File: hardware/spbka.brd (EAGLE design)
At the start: 33 x 20.3 mm, 20 parts, among them Q1 DMP1045U-7, U1 ATTINY10, U2 LM4041DYM3-1.2, U3 MCP6L01T

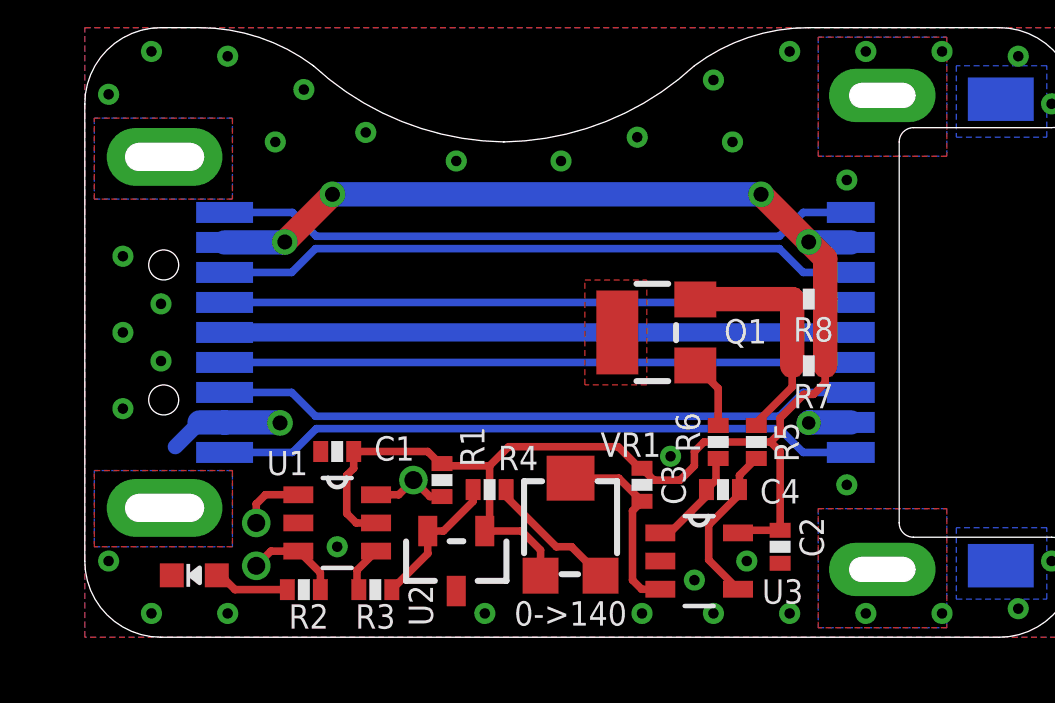
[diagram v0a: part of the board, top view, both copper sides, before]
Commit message: Some small changes, HW v1.2
Hardware bumped to v1.2:
Added unmasked vias for VCC and GND to make it easier to program.
Made USB3 socket pads longer (some components and things had to be moved slightly for this).
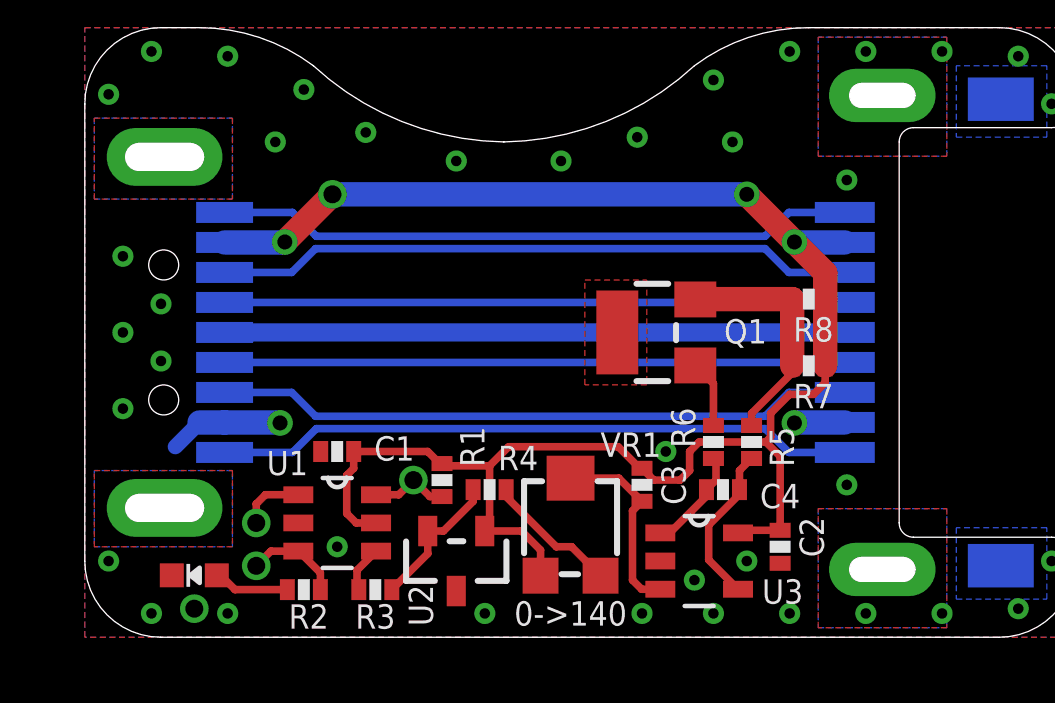
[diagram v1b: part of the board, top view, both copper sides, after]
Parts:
- moved R5 0.16 mm to (28.6, 33.2)
- moved R6 0.16 mm to (27.3, 33.2)
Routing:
- net GND: track 5.25 -> 5.52 mm, vias 40 -> 41
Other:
- board text added: "200411 1.2"
- board text removed: "190909 1.1"

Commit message: hardware v2.1
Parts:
- removed CN1: (no value), zak:USB-3-TYPE-A-SMD-PLUG-SLOT
- removed CN2: (no value), zak:USB-3-TYPE-A-SMD-SOCKET-SLOT
- removed U3: MCP6L01T, zak:SOT23-5_SM_PAD
- added Q2: MMBT4401 / MMBT3904, microbuilder:SOT23-R
- added R10: 10k, zak:0402_XSMALL
- added R11: 1k, zak:0402_XSMALL
- added R12: 1M, zak:0402_XSMALL
- added R9: 47k, zak:0402_XSMALL
- added USB1: USB-TYPE-AHORZ, zak:USB-TYPE-A
- added USB2: (no value), zak:USB-TYPE-A-PLUG-SLOT
- added VR2: 5k, zak:TRIMPOT_BOURNS3MM
- C1, C2, C3, C4, R2, R5, R6, R7, R8: device zak:0402_SMALL -> zak:0402_XSMALL
- Q1: value DMP1045U-7 -> DMP1045U-7 / DMP2035U-7
- R1: value 3k9 -> 10k; device zak:0402_SMALL -> zak:0402_XSMALL
- R3: value 3k9 -> 1k; device zak:0402_SMALL -> zak:0402_XSMALL
- R4: value 3k9 -> 0R; device zak:0402_SMALL -> zak:0402_XSMALL
- U2: value LM4041DYM3-1.2 -> MCP6L01T / MCP6001T; device zak:SOT-23-SLIMPAD -> zak:SOT23-5_SM_PAD
- moved U2 14.9 mm to (25.8, 42.3)
- moved R3 12.3 mm to (26.7, 34.3)
- moved R7 11.1 mm to (20.4, 40.4), turned to 0 degrees
- moved U1 11.1 mm to (13.4, 41.5), turned to 270 degrees
- moved C2 11.0 mm to (25.8, 40.0), turned to 180 degrees
- moved R2 10.3 mm to (8.30, 37.0), turned to 90 degrees
- moved R8 10.1 mm to (20.4, 38.8), turned to 0 degrees
- moved C1 8.90 mm to (15.8, 41.7), turned to 270 degrees
- moved LED1 8.79 mm to (7.00, 37.0), turned to 180 degrees
- moved VR1 8.45 mm to (14.1, 30.6), turned to 90 degrees
- moved R1 8.17 mm to (15.8, 39.7)
- moved R6 7.09 mm to (22.4, 38.3), turned to 270 degrees
- moved R4 7.02 mm to (26.7, 33.1), turned to 180 degrees
- moved R5 6.75 mm to (24.7, 38.7), turned to 180 degrees
- moved C4 6.59 mm to (24.7, 37.5)
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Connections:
- removed net N$13: R3.1, U1.4
- removed net N$14: CN1.SSTX-, CN2.SSTX-
- removed net N$15: CN1.D+, CN2.D+
- removed net N$16: CN1.D-, CN2.D-
- removed net N$19: C1.2, C2.2, C3.2, CN1.VBUS, CN2.VBUS, R1.2, R7.1, R8.1, U1.5, U2.1, U3.5, VR1.1
- removed net N$9 (its old number): CN1.SSRX-, CN2.SSRX-
- new net N$1: Q2.2, R3.2, R4.1
- new net VBUS: C1.2, C2.2, C3.2, Q2.1, Q2.3, R1.2, R10.2, R11.2, R7.1, R8.1, R9.2, U1.5, U2.5, USB1.VCC, USB2.VBUS, VR1.1
- net GND: now also U2.2, USB1.GND, USB1.SHIELD1, USB1.SHIELD2, USB2.GND, USB2.PAD1, USB2.PAD2; no longer CN1.GND, CN1.PAD1, CN1.PAD2, CN2.GND, CN2.PAD1, CN2.PAD2, CN2.PAD3, CN2.PAD4, U3.2
- net N$11: now also R12.2, R9.1, U2.3; no longer U3.3
- net N$12: now also R11.1, VR2.1; no longer CN1.SSTX+, CN2.SSTX+
- net N$3: now also U2.1; no longer U3.1
- net N$5: now also USB1.D+, USB2.D+; no longer CN1.GND_DRAIN, CN2.GND_DRAIN
- net N$6: now also USB1.D-, USB2.D-; no longer CN1.SSRX+, CN2.SSRX+
- net N$7: now also R12.1, R3.1, U1.4, VR2.3; no longer R3.2, R4.1, U2.2
- net N$8: now also R10.1, U2.4; no longer U3.4
- net TPID: now also VR2.2
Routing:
- net N$19: track 59.0 -> 0.00 mm, vias 4 -> 0
- net VBUS: track 0.00 -> 58.1 mm, vias 0 -> 3
- net N$11: track 6.51 -> 30.9 mm, vias 0 -> 2
- net N$9 (its old number): track 21.3 -> 0.00 mm
- net N$14: track 21.3 -> 0.00 mm
- net N$16: track 20.7 -> 0.00 mm
- net N$15: track 20.7 -> 0.00 mm
- net N$7: track 4.76 -> 24.6 mm, vias 0 -> 2
- net N$12: track 21.3 -> 6.17 mm
- net N$6: track 21.3 -> 8.25 mm
- net N$5: track 20.7 -> 8.25 mm
- net RST: track 2.63 -> 14.0 mm, vias 1 -> 2
- net N$9: track 4.47 -> 13.8 mm, vias 0 -> 2
- net TPIC: track 3.20 -> 11.3 mm
- net TPID: track 2.16 -> 9.94 mm
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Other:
- board size 33 x 20.3 mm -> 24.3 x 18 mm
- board text added: "0"
- board text added: "1"
- board text added: "140"
- board text added: "20"
- board text added: "230306 2.1"
- board text added: "A:"
- board text added: "C"
- board text added: "D"
- board text added: "G"
- board text added: "R"
- board text added: "S:"
- board text added: "SMART POWER BANK KEEP-ALIVE"
- board text added: "V"
- board text removed: "0->140"
- board text removed: "200411 1.2"
- board text removed: "Smart Power Bank Keep-Alive"
- board text removed: "USB 3.1"
